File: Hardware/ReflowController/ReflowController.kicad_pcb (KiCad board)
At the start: 4 copper layers, 160 x 100 mm, 154 parts, among them J101 2060-1452, J102 2060-1452, J103 2060-1453, J104 2060-1452, J105 2060-1452, J106 2060-1452, J107 2060-1452, J108 2060-1452, J109 2060-1452, J110 2060-1452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

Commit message: work on DRC
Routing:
- net /IO/HSS_1_OUT_+: track 28.9 -> 19.7 mm
- net /IO/HSS_2_OUT_+: track 24.4 -> 18.2 mm
- net /IO/HSS_3_OUT_+: track 26.1 -> 22.4 mm
- net /IO/HSS_4_OUT_+: track 33.0 -> 30.1 mm

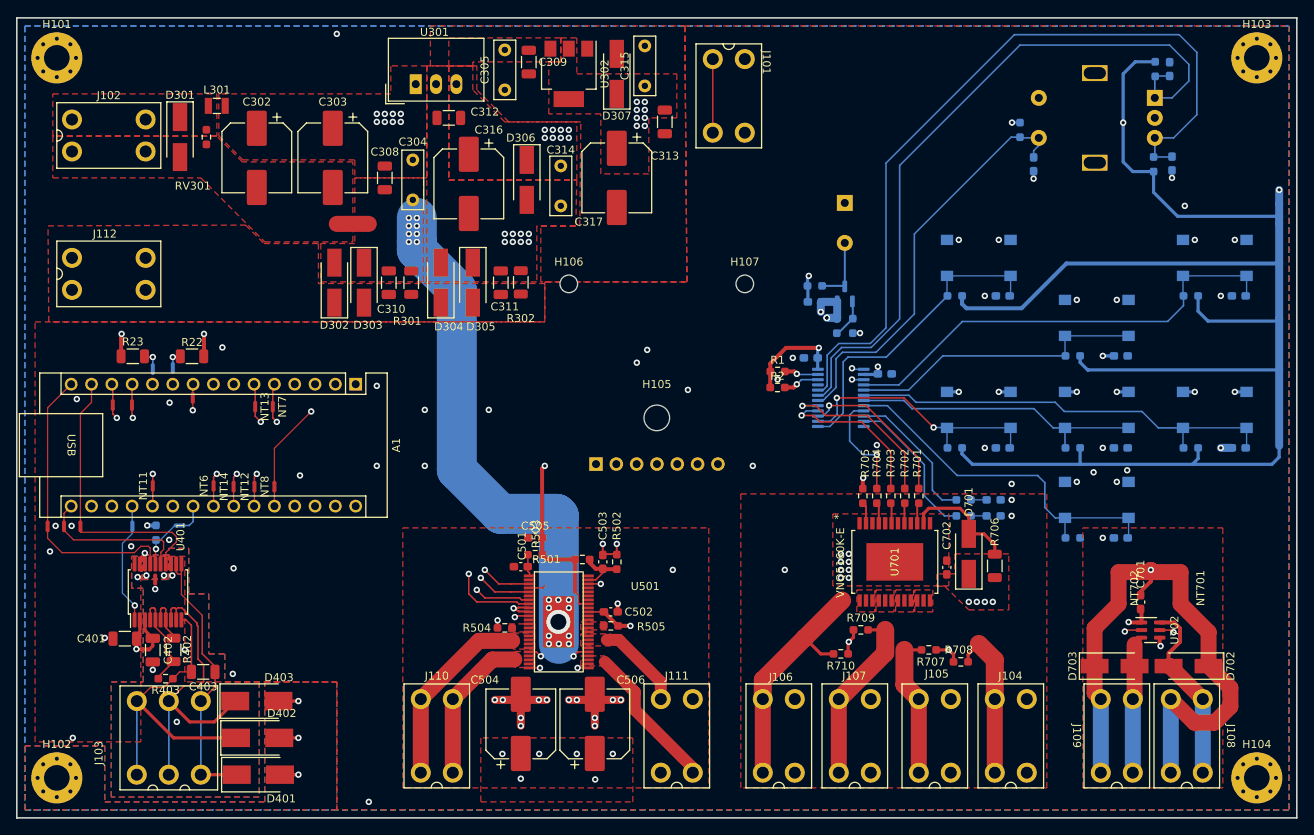
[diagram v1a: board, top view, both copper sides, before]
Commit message: Finished rewiev with Edwin, Need TO connect he HSS and DO the labeling
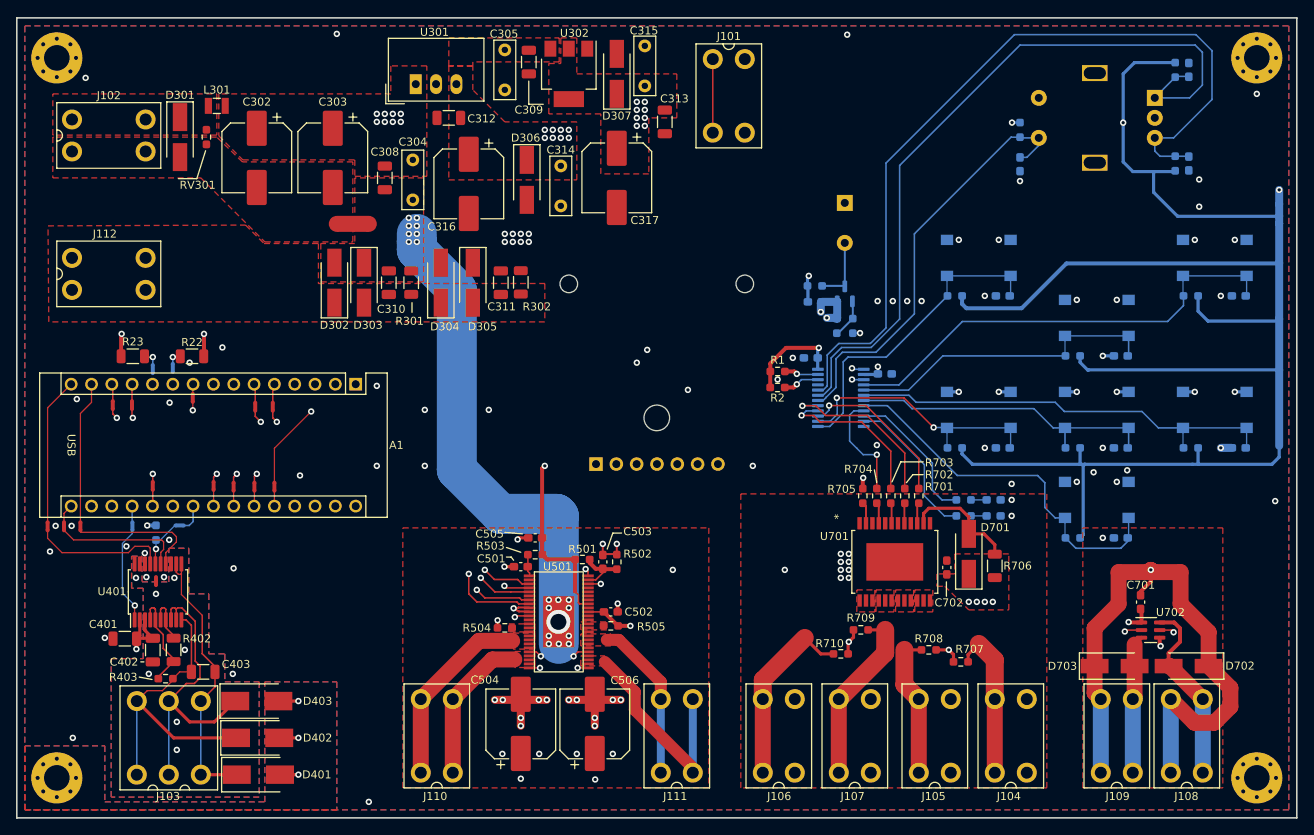
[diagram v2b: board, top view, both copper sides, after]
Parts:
- removed NT401: NetTie_2, NetTie:NetTie-2_SMD_Pad0.5mm
- U701: value VNQ5160K-E -> e
- moved R602 2.70 mm to (211.8, 58.2)
- moved R601 2.50 mm to (211.8, 46.5)
- moved C603 2.40 mm to (213.5, 46.5)
- moved C604 2.10 mm to (213.5, 58.2)
- moved C605 1.70 mm to (192.4, 58.3)
- moved NT402 0.22 mm to (84.4, 110.4)
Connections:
- C402 pad 1: Net-(U401-VDD) -> +3.3V
- U401 pad 3: Net-(U401-VDD) -> +3.3V
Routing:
- net +3.3V: track 583.8 -> 601.3 mm
- net /Fan Driver/FAN_2_OUT_-: track 18.5 -> 27.7 mm
- net /Fan Driver/FAN_2_OUT_+: track 11.1 -> 20.3 mm
- net /IO/HSS_4_OUT_+: track 30.1 -> 23.4 mm
- net /ui/ENCODER_A: track 90.6 -> 96.1 mm
- net GND: track 28.6 -> 33.4 mm, vias 66 -> 78
- net Net-(U401-VDD): track 4.29 -> 0.00 mm
- net /ui/ENCODER_B: track 100.0 -> 104.2 mm
- net /ui/BTN_SELECT: track 37.1 -> 39.6 mm
- net /ui/BTN_DOWN: track 37.5 -> 40.0 mm
- net GNDPWR: track 102.0 -> 100.0 mm
- net /~{UI_RESET}: track 81.5 -> 83.4 mm
- net /ui/ENCODER_SW: track 52.0 -> 53.2 mm
- net /ui/BTN_UP: track 45.9 -> 47.1 mm
- net /TemperatureReader/PT100_+OUT: track 39.6 -> 38.7 mm
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
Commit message: work on completion for first proto
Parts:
- R1, R2: value 4.7K -> 4k7; footprint Resistor_SMD:R_0603_1608Metric_Pad0.98x0.95mm_HandSolder -> Resistor_SMD:R_1206_3216Metric
- U701: value e -> VNQ5160K-E
- moved R2 0.56 mm to (161.7, 86.5)
- moved R1 0.54 mm to (161.7, 83.9)
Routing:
- net /IO/HSS_1_OUT_+: track 19.7 -> 28.5 mm
- net /IO/HSS_4_OUT_+: track 23.4 -> 30.6 mm
- net /IO/HSS_2_OUT_+: track 18.2 -> 20.9 mm
- net +3.3V: track 601.3 -> 603.0 mm
- net /uC/PF0: track 0.00 -> 1.54 mm
- net /uC/PF1: track 0.00 -> 1.41 mm
- net /HSS_1_EN: track 20.0 -> 20.8 mm
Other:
- board text added: "Reflow Controller 21082023"

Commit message: work on BOM cleanup
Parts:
- R604, R605: value 4.7K -> 4k7; footprint Resistor_SMD:R_0603_1608Metric_Pad0.98x0.95mm_HandSolder -> Resistor_SMD:R_1206_3216Metric
- moved R604 0.65 mm to (184.8, 102.7)
- moved R605 0.52 mm to (184.8, 100.2)
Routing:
- net /ui/LED_ALIVE: track 17.9 -> 17.0 mm
